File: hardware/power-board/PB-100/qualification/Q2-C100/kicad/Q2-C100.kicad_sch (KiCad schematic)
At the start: 34 parts

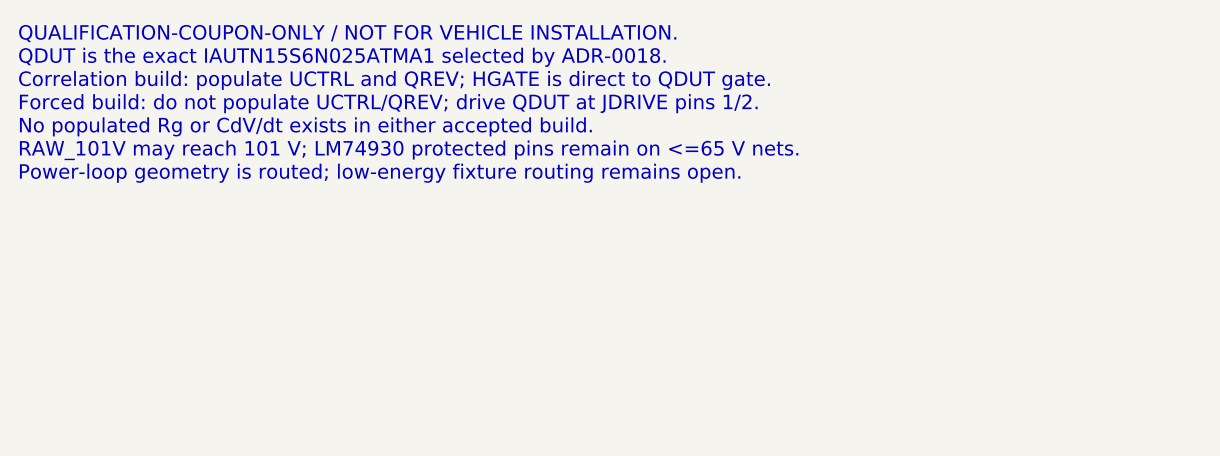
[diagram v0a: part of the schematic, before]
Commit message: feat(pb100): complete Q2 coupon electrical routing
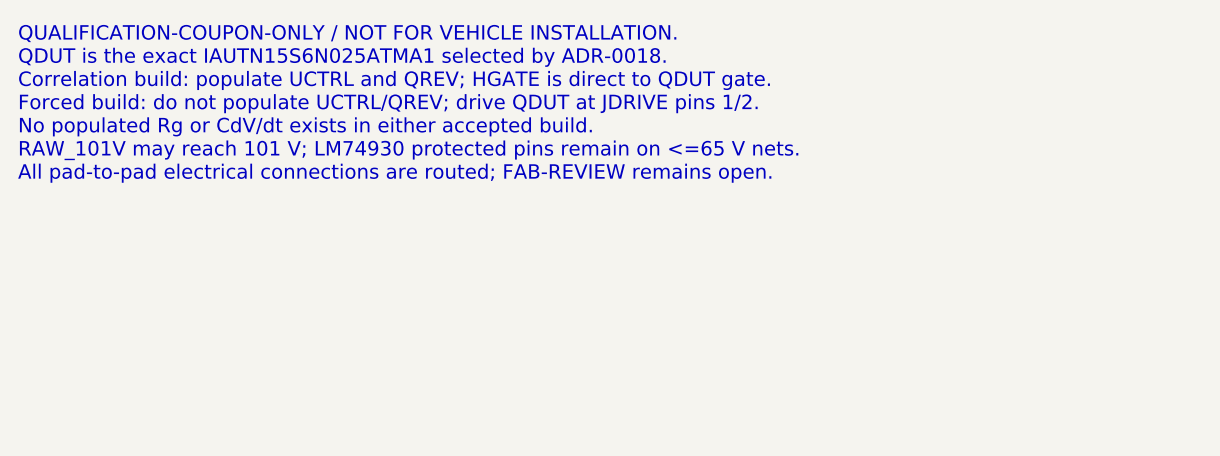
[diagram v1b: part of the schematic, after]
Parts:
- ROV1, ROV2: footprint Q2C100:R_C_0603_1608Metric -> Q2C100:R_1206_3216Metric
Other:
- note added: "QUALIFICATION-COUPON-ONLY / NOT FOR VEHICLE INSTALLATION. QDUT is the exact IAUTN15S6N025ATMA1 selected by ADR-0018. Correlation build: populate UCTRL and QREV; HGATE is direct to QDUT gate. Forced build: do not populate UCTRL/QREV; drive QDUT at JDRIVE pins 1/2. No populated Rg or CdV/dt exists in either accepted build. RAW_101V may reach 101 V; LM74930 protected pins remain on <=65 V nets. All 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"
- note removed: "QUALIFICATION-COUPON-ONLY / NOT FOR VEHICLE INSTALLATION. QDUT is the exact IAUTN15S6N025ATMA1 selected by ADR-0018. Correlation build: populate UCTRL and QREV; HGATE is direct to QDUT gate. Forced build: do not populate UCTRL/QREV; drive QDUT at JDRIVE pins 1/2. No populated Rg or CdV/dt exists in either accepted build. RAW_101V may reach 101 V; LM74930 protected pins remain on <=65 V nets. Powe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"
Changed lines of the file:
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@@
     (comment 2 "Generated deterministically from accepted contracts and component decisions.")
   )
-  (text "QUALIFICATION-COUPON-ONLY / NOT FOR VEHICLE INSTALLATION.\nQDUT is the exact IAUTN15S6N025ATMA1 selected by ADR-0018.\nCorrelation build: populate UCTRL and QREV; HGATE is direct to QDUT gate.\nForced build: do not populate UCTRL/QREV; drive QDUT at JDRIVE pins 1/2.\nNo populated Rg or CdV/dt exists in either accepted build.\nRAW_101V may reach 101 V; LM74930 protected pins remain on <=65 V nets.\nPower-loop geometry is routed; low-energy fixture routing remains open."
+  (text "QUALIFICATION-COUPON-ONLY / NOT FOR VEHICLE INSTALLATION.\nQDUT is the exact IAUTN15S6N025ATMA1 selected by ADR-0018.\nCorrelation build: populate UCTRL and QREV; HGATE is direct to QDUT gate.\nForced build: do not populate UCTRL/QREV; drive QDUT at JDRIVE pins 1/2.\nNo populated Rg or CdV/dt exists in either accepted build.\nRAW_101V may reach 101 V; LM74930 protected pins remain on <=65 V nets.\nAll pad-to-pad electrical connections are routed; FAB-REVIEW remains open."
     (at 20 20 0)
     (effects (font (size 1.6 1.6)) (justify left top))
@@
     (property "Reference" "ROV1" (at 76.20 414.02 0) (effects (font (size 1.27 1.27))))
     (property "Value" "42.2k 1% AEC-Q200" (at 76.20 416.56 0) (effects (font (size 1.27 1.27))))
-    (property "Footprint" "Q2C100:R_C_0603_1608Metric" (at 76.20 431.80 0) (effects (font (size 1.27 1.27)) hide))
+    (property "Footprint" "Q2C100:R_1206_3216Metric" (at 76.20 431.80 0) (effects (font (size 1.27 1.27)) hide))
     (property "Datasheet" "https://www.ti.com/lit/ds/symlink/lm74930-q1.pdf" (at 76.20 434.34 0) (effects (font (size 1.27 1.27)) hide))
     (pin "1")
@@
     (property "Reference" "ROV2" (at 76.20 462.28 0) (effects (font (size 1.27 1.27))))
     (property "Value" "42.2k 1% AEC-Q200" (at 76.20 464.82 0) (effects (font (size 1.27 1.27))))
-    (property "Footprint" "Q2C100:R_C_0603_1608Metric" (at 76.20 480.06 0) (effects (font (size 1.27 1.27)) hide))
+    (property "Footprint" "Q2C100:R_1206_3216Metric" (at 76.20 480.06 0) (effects (font (size 1.27 1.27)) hide))
     (property "Datasheet" "https://www.ti.com/lit/ds/symlink/lm74930-q1.pdf" (at 76.20 482.60 0) (effects (font (size 1.27 1.27)) hide))
     (pin "1")

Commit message: feat(q2): strengthen coupon pre-fab evidence
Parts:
- CCAP: value 100nF 25V X7R AEC-Q200 -> CGA3E2X7R1H104K080AE 100nF 50V X7R
- ROV1, ROV2: value 42.2k 1% AEC-Q200 -> CRCW120642K2FKEAHP 42.2k 1%
- ROV3: value 1.00k 1% AEC-Q200 -> CRCW06031K00FKEAHP 1.00k 1%
- RVS: value 10.0k 1% 1206 AEC-Q200 -> CRCW120610K0FKEAHP 10.0k 1%
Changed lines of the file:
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@@
     (dnp no)
     (property "Reference" "ROV1" (at 76.20 414.02 0) (effects (font (size 1.27 1.27))))
-    (property "Value" "42.2k 1% AEC-Q200" (at 76.20 416.56 0) (effects (font (size 1.27 1.27))))
+    (property "Value" "CRCW120642K2FKEAHP 42.2k 1%" (at 76.20 416.56 0) (effects (font (size 1.27 1.27))))
     (property "Footprint" "Q2C100:R_1206_3216Metric" (at 76.20 431.80 0) (effects (font (size 1.27 1.27)) hide))
-    (property "Datasheet" "https://www.ti.com/lit/ds/symlink/lm74930-q1.pdf" (at 76.20 434.34 0) (effects (font (size 1.27 1.27)) hide))
+    (property "Datasheet" "https://www.vishay.com/docs/20043/crcwhpe3.pdf" (at 76.20 434.34 0) (effects (font (size 1.27 1.27)) hide))
     (pin "1")
     (pin "2")
@@
     (dnp no)
     (property "Reference" "ROV2" (at 76.20 462.28 0) (effects (font (size 1.27 1.27))))
-    (property "Value" "42.2k 1% AEC-Q200" (at 76.20 464.82 0) (effects (font (size 1.27 1.27))))
+    (property "Value" "CRCW120642K2FKEAHP 42.2k 1%" (at 76.20 464.82 0) (effects (font (size 1.27 1.27))))
     (property "Footprint" "Q2C100:R_1206_3216Metric" (at 76.20 480.06 0) (effects (font (size 1.27 1.27)) hide))
-    (property "Datasheet" "https://www.ti.com/lit/ds/symlink/lm74930-q1.pdf" (at 76.20 482.60 0) (effects (font (size 1.27 1.27)) hide))
+    (property "Datasheet" "https://www.vishay.com/docs/20043/crcwhpe3.pdf" (at 76.20 482.60 0) (effects (font (size 1.27 1.27)) hide))
     (pin "1")
     (pin "2")
@@
     (dnp no)
     (property "Reference" "ROV3" (at 76.20 510.54 0) (effects (font (size 1.27 1.27))))
-    (property "Value" "1.00k 1% AEC-Q200" (at 76.20 513.08 0) (effects (font (size 1.27 1.27))))
+    (property "Value" "CRCW06031K00FKEAHP 1.00k 1%" (at 76.20 513.08 0) (effects (font (size 1.27 1.27))))
     (property "Footprint" "Q2C100:R_C_0603_1608Metric" (at 76.20 528.32 0) (effects (font (size 1.27 1.27)) hide))
-    (property "Datasheet" "https://www.ti.com/lit/ds/symlink/lm74930-q1.pdf" (at 76.20 530.86 0) (effects (font (size 1.27 1.27)) hide))
+    (property "Datasheet" "https://www.vishay.com/docs/20043/crcwhpe3.pdf" (at 76.20 530.86 0) (effects (font (size 1.27 1.27)) hide))
     (pin "1")
     (pin "2")
@@
     (dnp no)
     (property "Reference" "RVS" (at 76.20 558.80 0) (effects (font (size 1.27 1.27))))
-    (property "Value" "10.0k 1% 1206 AEC-Q200" (at 76.20 561.34 0) (effects (font (size 1.27 1.27))))
+    (property "Value" "CRCW120610K0FKEAHP 10.0k 1%" (at 76.20 561.34 0) (effects (font (size 1.27 1.27))))
     (property "Footprint" "Q2C100:R_1206_3216Metric" (at 76.20 576.58 0) (effects (font (size 1.27 1.27)) hide))
-    (property "Datasheet" "https://www.ti.com/lit/ds/symlink/lm74930-q1.pdf" (at 76.20 579.12 0) (effects (font (size 1.27 1.27)) hide))
+    (property "Datasheet" "https://www.vishay.com/docs/20043/crcwhpe3.pdf" (at 76.20 579.12 0) (effects (font (size 1.27 1.27)) hide))
     (pin "1")
     (pin "2")
@@
     (dnp no)
     (property "Reference" "CCAP" (at 185.42 109.22 0) (effects (font (size 1.27 1.27))))
-    (property "Value" "100nF 25V X7R AEC-Q200" (at 185.42 111.76 0) (effects (font (size 1.27 1.27))))
+    (property "Value" "CGA3E2X7R1H104K080AE 100nF 50V X7R" (at 185.42 111.76 0) (effects (font (size 1.27 1.27))))
     (property "Footprint" "Q2C100:R_C_0603_1608Metric" (at 185.42 127.00 0) (effects (font (size 1.27 1.27)) hide))
-    (property "Datasheet" "https://www.ti.com/lit/ds/symlink/lm74930-q1.pdf" (at 185.42 129.54 0) (effects (font (size 1.27 1.27)) hide))
+    (property "Datasheet" "https://product.tdk.com/en/search/capacitor/ceramic/mlcc/info?part_no=CGA3E2X7R1H104K080AE" (at 185.42 129.54 0) (effects (font (size 1.27 1.27)) hide))
     (pin "1")
     (pin "2")

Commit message: feat(q2): bind coupon fixture interfaces
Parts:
- JDRIVE: value FORCED_DRIVER_KELVIN -> 436500428 MICRO-FIT 4POS DRIVER; footprint Q2C100:PinHeader_1x04_P2.54 -> Q2C100:MicroFit_43650_0428_Vertical_R90
- JHEAT: value ISOLATED_CASE_HEATER -> 436500228 MICRO-FIT 2POS HEATER; footprint Q2C100:PinHeader_1x02_P2.54 -> Q2C100:MicroFit_43650_0228_Vertical
- JTEMP: value ISOLATED_TSEP_INPUT -> 436500328 MICRO-FIT 3POS TEMP; footprint Q2C100:PinHeader_1x02_P2.54 -> Q2C100:MicroFit_43650_0328_Vertical
- TPD: value QDUT_DRAIN_KELVIN -> S1751-46R QDUT_DRAIN_KELVIN; footprint Q2C100:TestPoint_Loop_1.0mm -> Q2C100:Harwin_S1751-46R
- TPFLT: value FAULT_PROBE -> S1751-46R FAULT_PROBE; footprint Q2C100:TestPoint_Loop_1.0mm -> Q2C100:Harwin_S1751-46R
- TPG: value QDUT_GATE_KELVIN -> S1751-46R QDUT_GATE_KELVIN; footprint Q2C100:TestPoint_Loop_1.0mm -> Q2C100:Harwin_S1751-46R
- TPGND: value PROBE_GND -> S1751-46R PROBE_GND; footprint Q2C100:TestPoint_Loop_1.0mm -> Q2C100:Harwin_S1751-46R
- TPHG: value UCTRL_HGATE_PROBE -> S1751-46R UCTRL_HGATE_PROBE; footprint Q2C100:TestPoint_Loop_1.0mm -> Q2C100:Harwin_S1751-46R
- TPOUT: value SYSTEM_OUT_PROBE -> S1751-46R SYSTEM_OUT_PROBE; footprint Q2C100:TestPoint_Loop_1.0mm -> Q2C100:Harwin_S1751-46R
- TPOV: value OV_TRIGGER_PROBE -> S1751-46R OV_TRIGGER_PROBE; footprint Q2C100:TestPoint_Loop_1.0mm -> Q2C100:Harwin_S1751-46R
- TPS: value QDUT_SOURCE_KELVIN -> S1751-46R QDUT_SOURCE_KELVIN; footprint Q2C100:TestPoint_Loop_1.0mm -> Q2C100:Harwin_S1751-46R
- TPVS: value CTRL_VS_PROBE -> S1751-46R CTRL_VS_PROBE; footprint Q2C100:TestPoint_Loop_1.0mm -> Q2C100:Harwin_S1751-46R
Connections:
- no-connect marks 6 -> 7
